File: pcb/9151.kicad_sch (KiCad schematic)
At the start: 22 parts, among them J10 JAE_SIM_Card_SF72S006, J5 Conn_ARM_SWD_TagConnect_TC203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, J9 Conn_Coaxial, U1 nRF9151-LAXX, U3 W25Q128JVP, U4 TPD3F303DPV

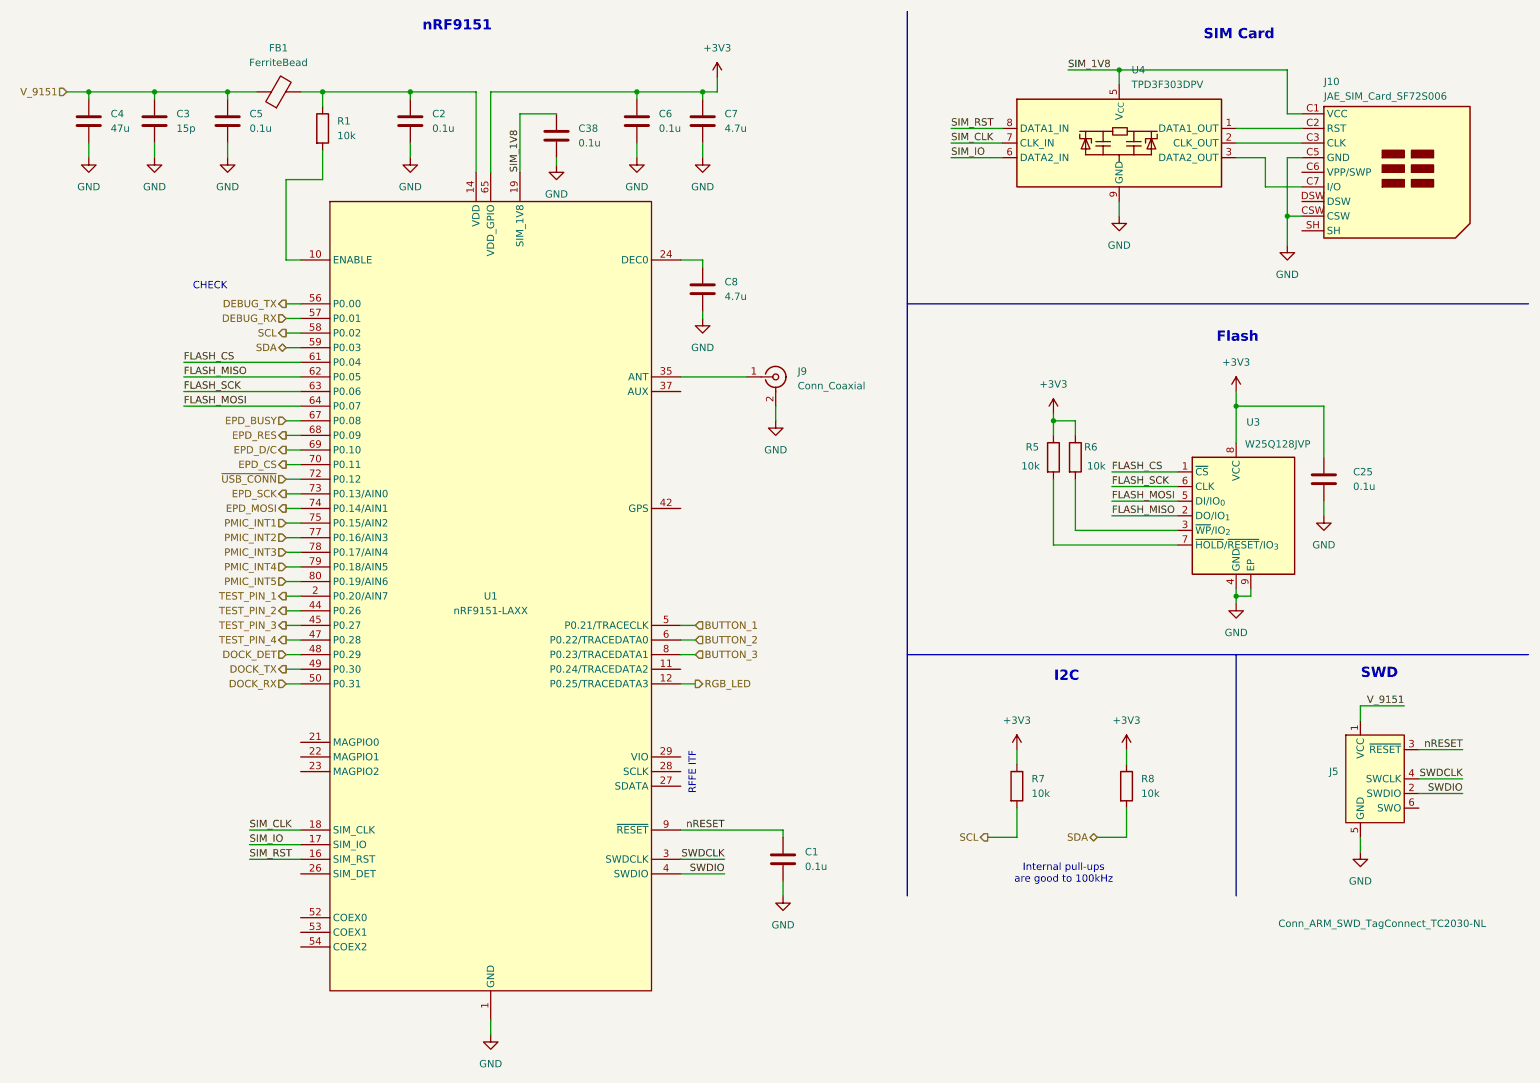
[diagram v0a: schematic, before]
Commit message: Fix display sch
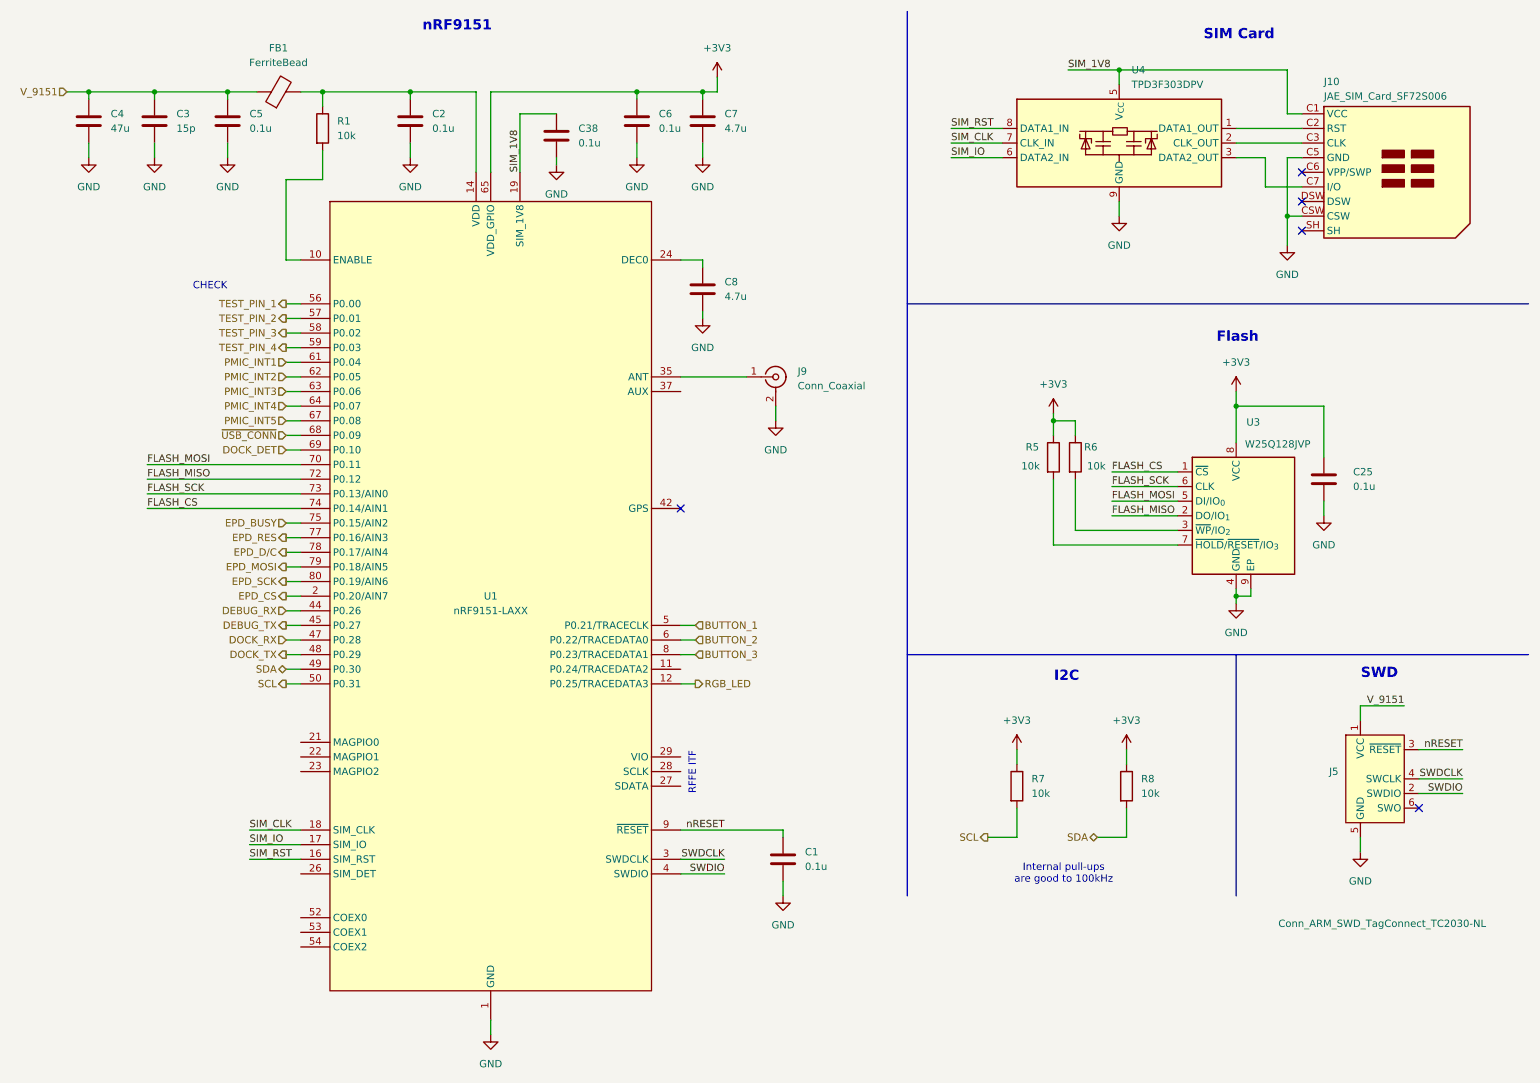
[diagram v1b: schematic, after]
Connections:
- net DEBUG_RX: now also U1.44 (P0.26); no longer U1.57 (P0.01)
- net DEBUG_TX: now also U1.45 (P0.27); no longer U1.56 (P0.00)
- net DOCK_DET: now also U1.69 (P0.10); no longer U1.48 (P0.29)
- net DOCK_RX: now also U1.47 (P0.28); no longer U1.50 (P0.31)
- net DOCK_TX: now also U1.48 (P0.29); no longer U1.49 (P0.30)
- net EPD_BUSY: now also U1.75 (P0.15/AIN2); no longer U1.67 (P0.08)
- net EPD_CS: now also U1.2 (P0.20/AIN7); no longer U1.70 (P0.11)
- net EPD_D/C: now also U1.78 (P0.17/AIN4); no longer U1.69 (P0.10)
- net EPD_MOSI: now also U1.79 (P0.18/AIN5); no longer U1.74 (P0.14/AIN1)
- net EPD_RES: now also U1.77 (P0.16/AIN3); no longer U1.68 (P0.09)
- net EPD_SCK: now also U1.80 (P0.19/AIN6); no longer U1.73 (P0.13/AIN0)
- net FLASH_CS: now also U1.74 (P0.14/AIN1); no longer U1.61 (P0.04)
- net FLASH_MISO: now also U1.72 (P0.12); no longer U1.62 (P0.05)
- net FLASH_MOSI: now also U1.70 (P0.11); no longer U1.64 (P0.07)
- net FLASH_SCK: now also U1.73 (P0.13/AIN0); no longer U1.63 (P0.06)
- net PMIC_INT1: now also U1.61 (P0.04); no longer U1.75 (P0.15/AIN2)
- net PMIC_INT2: now also U1.62 (P0.05); no longer U1.77 (P0.16/AIN3)
- net PMIC_INT3: now also U1.63 (P0.06); no longer U1.78 (P0.17/AIN4)
- net PMIC_INT4: now also U1.64 (P0.07); no longer U1.79 (P0.18/AIN5)
- net PMIC_INT5: now also U1.67 (P0.08); no longer U1.80 (P0.19/AIN6)
- net SCL: now also U1.50 (P0.31); no longer U1.58 (P0.02)
- net SDA: now also U1.49 (P0.30); no longer U1.59 (P0.03)
- net TEST_PIN_1: now also U1.56 (P0.00); no longer U1.2 (P0.20/AIN7)
- net TEST_PIN_2: now also U1.57 (P0.01); no longer U1.44 (P0.26)
- net TEST_PIN_3: now also U1.58 (P0.02); no longer U1.45 (P0.27)
- net TEST_PIN_4: now also U1.59 (P0.03); no longer U1.47 (P0.28)
- net ~{USB_CONN}: now also U1.68 (P0.09); no longer U1.72 (P0.12)
- no-connect marks 0 -> 5
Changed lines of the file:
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@@
 		(color 0 0 0 0)
 	)
+	(no_connect
+		(at 245.11 40.64)
+	)
+	(no_connect
+		(at 245.11 45.72)
+	)
+	(no_connect
+		(at 245.11 50.8)
+	)
+	(no_connect
+		(at 137.16 99.06)
+	)
+	(no_connect
+		(at 265.43 151.13)
+	)
 	(polyline
 		(pts
@@
 	(wire
 		(pts
+			(xy 44.45 99.06) (xy 71.12 99.06)
+		)
+		(stroke
+			(width 0)
+			(type default)
+		)
+	)
+	(wire
+		(pts
 			(xy 212.09 92.71) (xy 223.52 92.71)
 		)
@@
 	(wire
 		(pts
-			(xy 50.8 76.2) (xy 71.12 76.2)
-		)
-		(stroke
-			(width 0)
-			(type default)
-		)
-	)
-	(wire
-		(pts
 			(xy 233.68 113.03) (xy 233.68 114.3)
 		)
@@
 	(wire
 		(pts
+			(xy 44.45 93.98) (xy 71.12 93.98)
+		)
+		(stroke
+			(width 0)
+			(type default)
+		)
+	)
+	(wire
+		(pts
 			(xy 68.58 63.5) (xy 71.12 63.5)
 		)
@@
 	(wire
 		(pts
-			(xy 68.58 91.44) (xy 71.12 91.44)
+			(xy 68.58 81.28) (xy 71.12 81.28)
 		)
 		(stroke
@@
 	(wire
 		(pts
-			(xy 68.58 96.52) (xy 71.12 96.52)
-		)
-		(stroke
-			(width 0)
-			(type default)
-		)
-	)
-	(wire
-		(pts
 			(xy 154.94 156.21) (xy 154.94 154.94)
 		)
@@
 	(wire
 		(pts
+			(xy 68.58 78.74) (xy 71.12 78.74)
+		)
+		(stroke
+			(width 0)
+			(type default)
+		)
+	)
+	(wire
+		(pts
 			(xy 68.58 109.22) (xy 71.12 109.22)
 		)
@@
 	(wire
 		(pts
-			(xy 68.58 99.06) (xy 71.12 99.06)
-		)
-		(stroke
-			(width 0)
-			(type default)
-		)
-	)
-	(wire
-		(pts
 			(xy 68.58 66.04) (xy 71.12 66.04)
 		)
@@
 	(wire
 		(pts
+			(xy 44.45 91.44) (xy 71.12 91.44)
+		)
+		(stroke
+			(width 0)
+			(type default)
+		)
+	)
+	(wire
+		(pts
+			(xy 44.45 96.52) (xy 71.12 96.52)
+		)
+		(stroke
+			(width 0)
+			(type default)
+		)
+	)
+	(wire
+		(pts
 			(xy 90.17 26.67) (xy 101.6 26.67)
 		)
@@
 	(wire
 		(pts
-			(xy 50.8 73.66) (xy 71.12 73.66)
-		)
-		(stroke
-			(width 0)
-			(type default)
-		)
-	)
-	(wire
-		(pts
 			(xy 201.93 105.41) (xy 223.52 105.41)
 		)
@@
 	(wire
 		(pts
-			(xy 68.58 93.98) (xy 71.12 93.98)
-		)
-		(stroke
-			(width 0)
-			(type default)
-		)
-	)
-	(wire
-		(pts
 			(xy 58.42 35.56) (xy 58.42 38.1)
 		)
@@
 	(wire
 		(pts
+			(xy 68.58 73.66) (xy 71.12 73.66)
+		)
+		(stroke
+			(width 0)
+			(type default)
+		)
+	)
+	(wire
+		(pts
 			(xy 68.58 119.38) (xy 71.12 119.38)
 		)
@@
 	(wire
 		(pts
-			(xy 50.8 78.74) (xy 71.12 78.74)
-		)
-		(stroke
-			(width 0)
-			(type default)
-		)
-	)
-	(wire
-		(pts
-			(xy 50.8 81.28) (xy 71.12 81.28)
+			(xy 68.58 76.2) (xy 71.12 76.2)
 		)
 		(stroke
@@
 	)
 	(label "FLASH_SCK"
-		(at 50.8 78.74 0)
+		(at 44.45 96.52 0)
 		(effects
 			(font
@@
 	)
 	(label "FLASH_CS"
-		(at 50.8 73.66 0)
+		(at 44.45 99.06 0)
 		(effects
 			(font
@@
 	)
 	(label "FLASH_MOSI"
-		(at 50.8 81.28 0)
+		(at 44.45 91.44 0)
 		(effects
 			(font
@@
 	)
 	(label "FLASH_MISO"
-		(at 50.8 76.2 0)
+		(at 44.45 93.98 0)
 		(effects
 			(font
@@
 	(hierarchical_label "PMIC_INT5"
 		(shape input)
-		(at 68.58 111.76 180)
+		(at 68.58 83.82 180)
 		(effects
 			(font
@@
 	(hierarchical_label "EPD_RES"
 		(shape output)
-		(at 68.58 86.36 180)
+		(at 68.58 104.14 180)
 		(effects
 			(font
@@
 	(hierarchical_label "DEBUG_RX"
 		(shape input)
-		(at 68.58 66.04 180)
+		(at 68.58 116.84 180)
 		(effects
 			(font
@@
 	(hierarchical_label "EPD_D{slash}C"
 		(shape output)
-		(at 68.58 88.9 180)
+		(at 68.58 106.68 180)
 		(effects
 			(font
@@
 	(hierarchical_label "DOCK_RX"
 		(shape input)
-		(at 68.58 129.54 180)
+		(at 68.58 121.92 180)
 		(effects
 			(font
@@
 	(hierarchical_label "DOCK_TX"
 		(shape output)
-		(at 68.58 127 180)
+		(at 68.58 124.46 180)
 		(effects
 			(font
@@
 	(hierarchical_label "TEST_PIN_3"
 		(shape output)
-		(at 68.58 119.38 180)
+		(at 68.58 68.58 180)
 		(effects
 			(font
@@
 	(hierarchical_label "TEST_PIN_1"
 		(shape output)
-		(at 68.58 114.3 180)
+		(at 68.58 63.5 180)
 		(effects
 			(font
@@
 	(hierarchical_label "SCL"
 		(shape output)
-		(at 68.58 68.58 180)
+		(at 68.58 129.54 180)
 		(effects
 			(font
@@
 	(hierarchical_label "DOCK_DET"
 		(shape input)
-		(at 68.58 124.46 180)
+		(at 68.58 88.9 180)
 		(effects
 			(font
@@
 	(hierarchical_label "TEST_PIN_2"
 		(shape output)
-		(at 68.58 116.84 180)
+		(at 68.58 66.04 180)
 		(effects
 			(font
@@
 	(hierarchical_label "~{USB_CONN}"
 		(shape input)
-		(at 68.58 93.98 180)
+		(at 68.58 86.36 180)
 		(effects
 			(font
@@
 	(hierarchical_label "PMIC_INT4"
 		(shape input)
-		(at 68.58 109.22 180)
+		(at 68.58 81.28 180)
 		(effects
 			(font
@@
 	(hierarchical_label "DEBUG_TX"
 		(shape output)
-		(at 68.58 63.5 180)
+		(at 68.58 119.38 180)
 		(effects
 			(font
@@
 	(hierarchical_label "EPD_BUSY"
 		(shape input)
-		(at 68.58 83.82 180)
+		(at 68.58 101.6 180)
 		(effects
 			(font
@@
 	(hierarchical_label "PMIC_INT3"
 		(shape input)
-		(at 68.58 106.68 180)
+		(at 68.58 78.74 180)
 		(effects
 			(font
@@
 	(hierarchical_label "SDA"
 		(shape bidirectional)
-		(at 68.58 71.12 180)
+		(at 68.58 127 180)
 		(effects
 			(font
@@
 	(hierarchical_label "TEST_PIN_4"
 		(shape output)
-		(at 68.58 121.92 180)
+		(at 68.58 71.12 180)
 		(effects
 			(font
@@
 	(hierarchical_label "EPD_SCK"
 		(shape output)
-		(at 68.58 96.52 180)
+		(at 68.58 111.76 180)
 		(effects
 			(font
@@
 	(hierarchical_label "EPD_MOSI"
 		(shape output)
-		(at 68.58 99.06 180)
+		(at 68.58 109.22 180)
 		(effects
 			(font
@@
 	(hierarchical_label "EPD_CS"
 		(shape output)
-		(at 68.58 91.44 180)
+		(at 68.58 114.3 180)
 		(effects
 			(font
@@
 	(hierarchical_label "PMIC_INT1"
 		(shape input)
-		(at 68.58 101.6 180)
+		(at 68.58 73.66 180)
 		(effects
 			(font
@@
 	(hierarchical_label "PMIC_INT2"
 		(shape input)
-		(at 68.58 104.14 180)
-		(effects
-			(font
+		(at 68.58 76.2 180)
+		(effects
+			(font

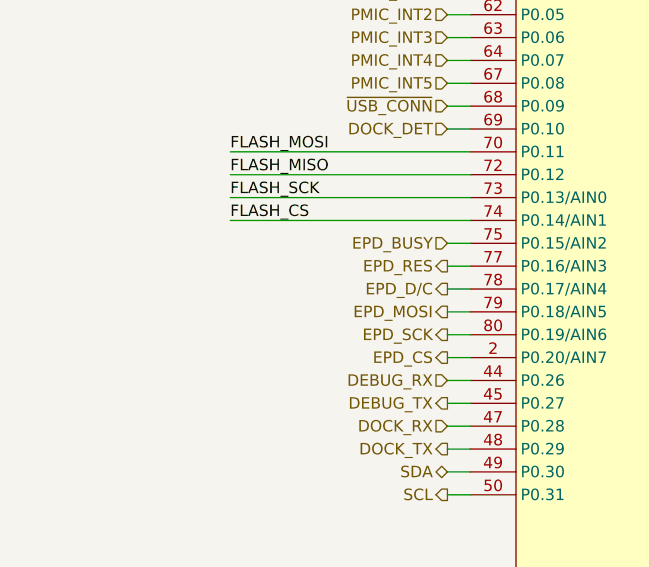
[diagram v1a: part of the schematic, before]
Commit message: Bus for epaper
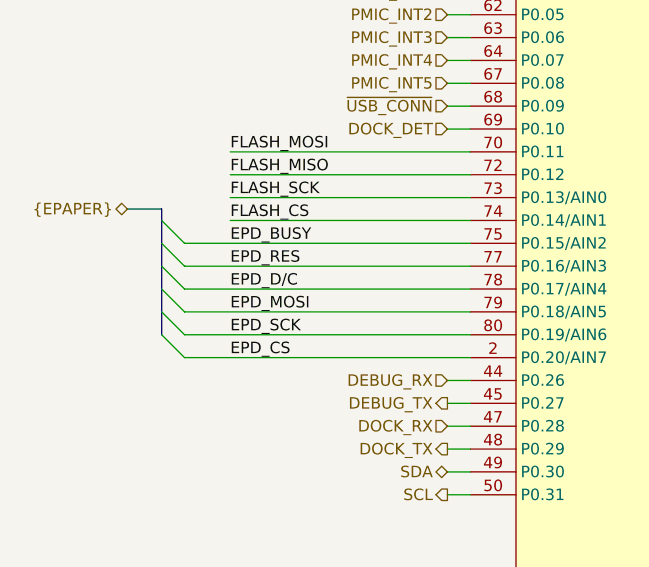
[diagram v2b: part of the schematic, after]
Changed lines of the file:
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@@
 		(at 265.43 151.13)
 	)
+	(bus_entry
+		(at 36.83 111.76)
+		(size 2.54 2.54)
+		(stroke
+			(width 0)
+			(type default)
+		)
+	)
+	(bus_entry
+		(at 36.83 109.22)
+		(size 2.54 2.54)
+		(stroke
+			(width 0)
+			(type default)
+		)
+	)
+	(bus_entry
+		(at 36.83 106.68)
+		(size 2.54 2.54)
+		(stroke
+			(width 0)
+			(type default)
+		)
+	)
+	(bus_entry
+		(at 36.83 101.6)
+		(size 2.54 2.54)
+		(stroke
+			(width 0)
+			(type default)
+		)
+	)
+	(bus_entry
+		(at 36.83 99.06)
+		(size 2.54 2.54)
+		(stroke
+			(width 0)
+			(type default)
+		)
+	)
+	(bus_entry
+		(at 36.83 104.14)
+		(size 2.54 2.54)
+		(stroke
+			(width 0)
+			(type default)
+		)
+	)
 	(polyline
 		(pts
@@
 		)
 	)
+	(bus
+		(pts
+			(xy 36.83 97.79) (xy 36.83 99.06)
+		)
+		(stroke
+			(width 0)
+			(type default)
+		)
+	)
 	(wire
 		(pts
@@
 		)
 	)
+	(bus
+		(pts
+			(xy 36.83 109.22) (xy 36.83 111.76)
+		)
+		(stroke
+			(width 0)
+			(type default)
+		)
+	)
 	(wire
 		(pts
@@
 		)
 	)
+	(bus
+		(pts
+			(xy 33.02 97.79) (xy 36.83 97.79)
+		)
+		(stroke
+			(width 0)
+			(type default)
+		)
+	)
 	(wire
 		(pts
@@
 	(wire
 		(pts
+			(xy 39.37 111.76) (xy 71.12 111.76)
+		)
+		(stroke
+			(width 0)
+			(type default)
+		)
+	)
+	(wire
+		(pts
 			(xy 140.97 26.67) (xy 140.97 27.94)
 		)
@@
 		)
 	)
+	(bus
+		(pts
+			(xy 36.83 101.6) (xy 36.83 104.14)
+		)
+		(stroke
+			(width 0)
+			(type default)
+		)
+	)
 	(wire
 		(pts
@@
 	(wire
 		(pts
-			(xy 68.58 104.14) (xy 71.12 104.14)
-		)
-		(stroke
-			(width 0)
-			(type default)
-		)
-	)
-	(wire
-		(pts
 			(xy 205.74 83.82) (xy 205.74 86.36)
 		)
@@
 	(wire
 		(pts
-			(xy 68.58 109.22) (xy 71.12 109.22)
-		)
-		(stroke
-			(width 0)
-			(type default)
-		)
-	)
-	(wire
-		(pts
 			(xy 214.63 151.13) (xy 214.63 156.21)
 		)
@@
 	(wire
 		(pts
-			(xy 68.58 101.6) (xy 71.12 101.6)
-		)
-		(stroke
-			(width 0)
-			(type default)
-		)
-	)
-	(wire
-		(pts
 			(xy 101.6 40.64) (xy 101.6 26.67)
 		)
@@
 		)
 	)
-	(wire
-		(pts
-			(xy 68.58 111.76) (xy 71.12 111.76)
+	(bus
+		(pts
+			(xy 36.83 104.14) (xy 36.83 106.68)
 		)
 		(stroke
@@
 		)
 	)
+	(bus
+		(pts
+			(xy 36.83 106.68) (xy 36.83 109.22)
+		)
+		(stroke
+			(width 0)
+			(type default)
+		)
+	)
 	(wire
 		(pts
@@
 	(wire
 		(pts
+			(xy 39.37 114.3) (xy 71.12 114.3)
+		)
+		(stroke
+			(width 0)
+			(type default)
+		)
+	)
+	(wire
+		(pts
 			(xy 255.27 135.89) (xy 255.27 133.35)
 		)
@@
 	(wire
 		(pts
+			(xy 39.37 109.22) (xy 71.12 109.22)
+		)
+		(stroke
+			(width 0)
+			(type default)
+		)
+	)
+	(wire
+		(pts
 			(xy 58.42 35.56) (xy 58.42 38.1)
 		)
@@
 	(wire
 		(pts
-			(xy 68.58 114.3) (xy 71.12 114.3)
-		)
-		(stroke
-			(width 0)
-			(type default)
-		)
-	)
-	(wire
-		(pts
 			(xy 62.23 160.02) (xy 71.12 160.02)
 		)
@@
 		)
 	)
+	(bus
+		(pts
+			(xy 36.83 99.06) (xy 36.83 101.6)
+		)
+		(stroke
+			(width 0)
+			(type default)
+		)
+	)
 	(polyline
 		(pts
@@
 		)
 	)
+	(wire
+		(pts
+			(xy 39.37 101.6) (xy 71.12 101.6)
+		)
+		(stroke
+			(width 0)
+			(type default)
+		)
+	)
 	(polyline
 		(pts
@@
 	(wire
 		(pts
+			(xy 39.37 106.68) (xy 71.12 106.68)
+		)
+		(stroke
+			(width 0)
+			(type default)
+		)
+	)
+	(wire
+		(pts
 			(xy 255.27 156.21) (xy 255.27 158.75)
 		)
@@
 	(wire
 		(pts
-			(xy 68.58 106.68) (xy 71.12 106.68)
+			(xy 39.37 104.14) (xy 71.12 104.14)
 		)
 		(stroke
@@
 		)
 	)
+	(label "EPD_RES"
+		(at 44.45 104.14 0)
+		(effects
+			(font
+				(size 1.27 1.27)
+			)
+			(justify left bottom)
+		)
+	)
 	(label "SWDIO"
 		(at 144.78 162.56 180)
@@
 		)
 	)
+	(label "EPD_D{slash}C"
+		(at 44.45 106.68 0)
+		(effects
+			(font
+				(size 1.27 1.27)
+			)
+			(justify left bottom)
+		)
+	)
 	(label "FLASH_CS"
 		(at 44.45 99.06 0)
@@
 		)
 	)
+	(label "EPD_CS"
+		(at 44.45 114.3 0)
+		(effects
+			(font
+				(size 1.27 1.27)
+			)
+			(justify left bottom)
+		)
+	)
 	(label "SIM_RST"
 		(at 62.23 160.02 0)
@@
 		)
 	)
+	(label "EPD_BUSY"
+		(at 44.45 101.6 0)
+		(effects
+			(font
+				(size 1.27 1.27)
+			)
+			(justify left bottom)
+		)
+	)
 	(label "FLASH_SCK"
 		(at 212.09 95.25 0)
@@
 		)
 	)
+	(label "EPD_MOSI"
+		(at 44.45 109.22 0)
+		(effects
+			(font
+				(size 1.27 1.27)
+			)
+			(justify left bottom)
+		)
+	)
 	(label "SIM_IO"
 		(at 62.23 157.48 0)
@@
 	(label "FLASH_CS"
 		(at 212.09 92.71 0)
+		(effects
+			(font
+				(size 1.27 1.27)
+			)
+			(justify left bottom)
+		)
+	)
+	(label "EPD_SCK"
+		(at 44.45 111.76 0)
 		(effects
 			(font
@@
 		)
 	)
-	(hierarchical_label "EPD_RES"
-		(shape output)
-		(at 68.58 104.14 180)
-		(effects
-			(font
-				(size 1.27 1.27)
-			)
-			(justify right)
-		)
-	)
 	(hierarchical_label "DEBUG_RX"
 		(shape input)
@@
 		)
 	)
-	(hierarchical_label "EPD_D{slash}C"
-		(shape output)
-		(at 68.58 106.68 180)
-		(effects
-			(font
-				(size 1.27 1.27)
-			)
-			(justify right)
-		)
-	)
 	(hierarchical_label "DOCK_RX"
 		(shape input)
@@
 		)
 	)
-	(hierarchical_label "EPD_BUSY"
-		(shape input)
-		(at 68.58 101.6 180)
-		(effects
-			(font
-				(size 1.27 1.27)
-			)
-			(justify right)
-		)
-	)
 	(hierarchical_label "PMIC_INT3"
 		(shape input)
@@
 		)
 	)
+	(hierarchical_label "{EPAPER}"
+		(shape bidirectional)
+		(at 33.02 97.79 180)
+		(effects
+			(font
+				(size 1.27 1.27)
+			)
+			(justify right)
+		)
+	)
 	(hierarchical_label "BUTTON_3"
 		(shape input)
@@
 		)
 	)
-	(hierarchical_label "EPD_SCK"
-		(shape output)
-		(at 68.58 111.76 180)
-		(effects
-			(font
-				(size 1.27 1.27)
-			)
-			(justify right)
-		)
-	)
-	(hierarchical_label "EPD_MOSI"
-		(shape output)
-		(at 68.58 109.22 180)
-		(effects
-			(font
-				(size 1.27 1.27)
-			)
-			(justify right)
-		)
-	)
-	(hierarchical_label "EPD_CS"
-		(shape output)
-		(at 68.58 114.3 180)
-		(effects
-			(font
-				(size 1.27 1.27)
-			)
-			(justify right)
-		)
-	)
